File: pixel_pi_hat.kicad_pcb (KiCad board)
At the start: 2 copper layers, 65 x 30 mm, 8 parts, among them J1 Conn_01x02_Male, J2 Conn_01x03_Male, J3 Conn_02x20_Odd_Even, U1 74125

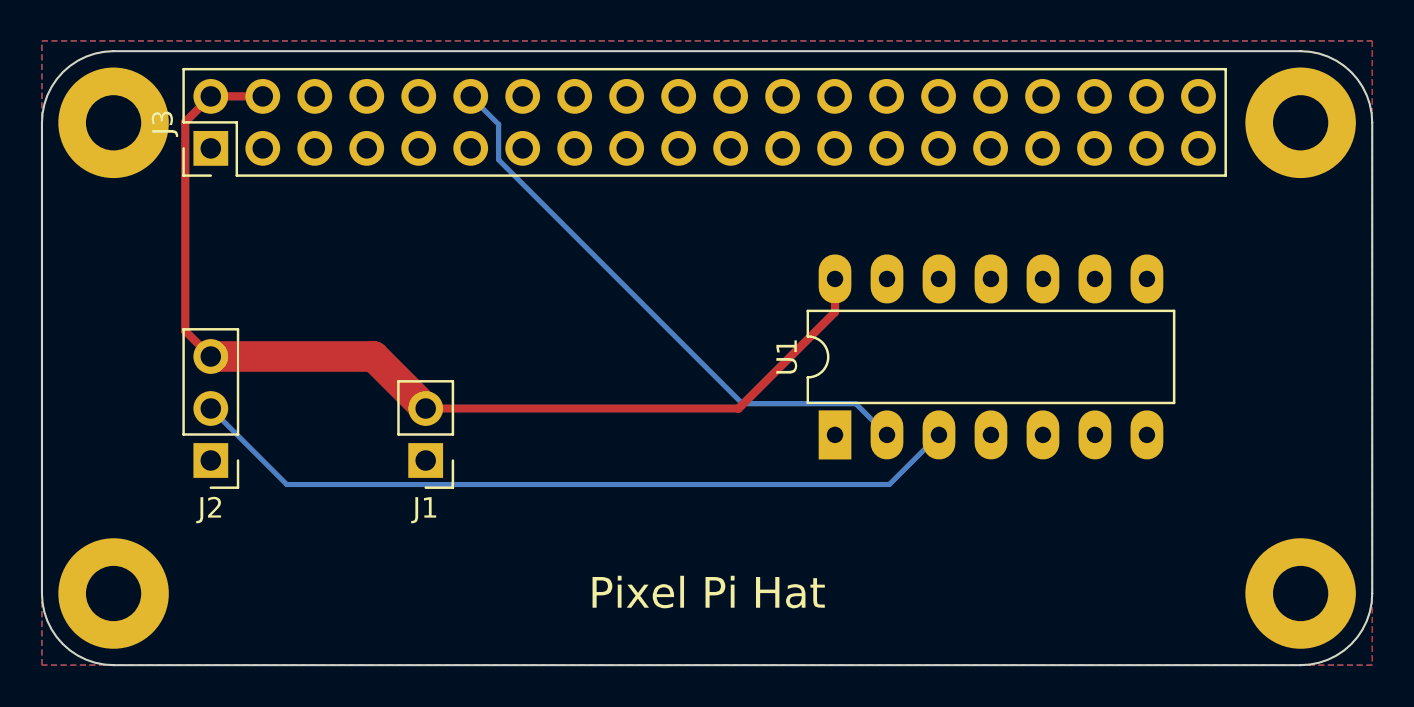
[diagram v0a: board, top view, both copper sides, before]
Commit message: Change to wago 804 push button terminals
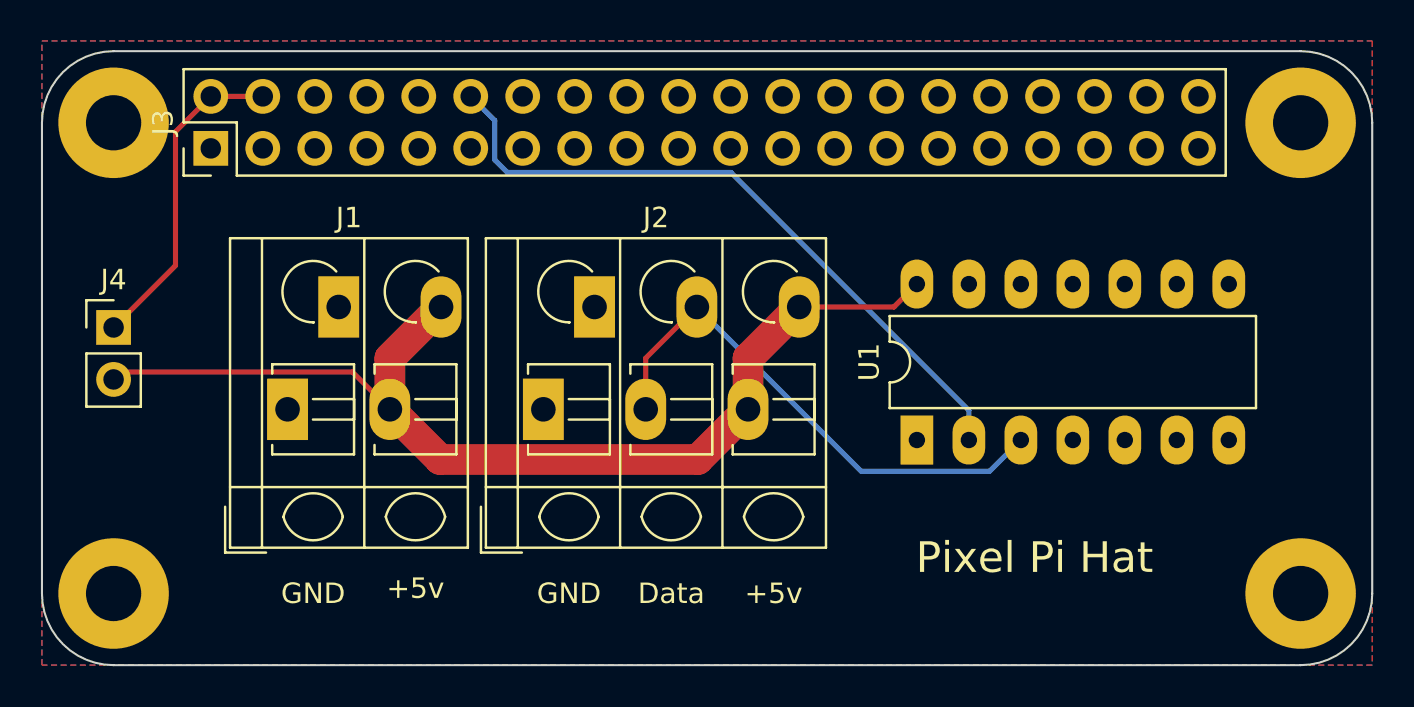
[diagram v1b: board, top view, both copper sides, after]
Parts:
- added J4: Conn_01x02_Male, Connector_PinHeader_2.54mm:PinHeader_1x02_P2.54mm_Vertical, F.Cu at (53.5, 49.0)
- J1: footprint Connector_PinHeader_2.54mm:PinHeader_1x02_P2.54mm_Vertical -> TerminalBlock_WAGO:TerminalBlock_WAGO_804-102_1x02_P5.00mm_45Degree
- J2: footprint Connector_PinHeader_2.54mm:PinHeader_1x03_P2.54mm_Vertical -> TerminalBlock_WAGO:TerminalBlock_WAGO_804-103_1x03_P5.00mm_45Degree
- moved J2 16.4 mm to (74.5, 53.0), turned to 0 degrees
- moved J1 7.20 mm to (62.0, 53.0), turned to 0 degrees
- moved U1 4.01 mm to (92.8, 54.5)
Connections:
- J3 pad 2: +5V -> Net-(J3-Pad2)
- J3 pad 4: +5V -> Net-(J3-Pad2)
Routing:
- net Net-(J3-Pad2): track 0.00 -> 15.8 mm
- net Net-(J2-Pad2): track 38.1 -> 25.8 mm
- net Net-(J3-Pad12): track 28.2 -> 33.3 mm
- net +5V: track 51.4 -> 52.2 mm
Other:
- board text added: "+5v"
- board text added: "Data"
- board text added: "GND"
